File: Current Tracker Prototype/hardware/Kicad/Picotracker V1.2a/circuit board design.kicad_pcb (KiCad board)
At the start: 2 copper layers, 33.3 x 20.1 mm, 31 parts, among them J1 Conn_01x10, J2 GND, J3 3.3V, J4 ICSS Logo, J5 Conn_01x01, Q1 IRLML6402, SW1 SW_Push, U1 MAX-M8C, U3 CMWX1ZZABZ-078, U6 MS5607-02BA

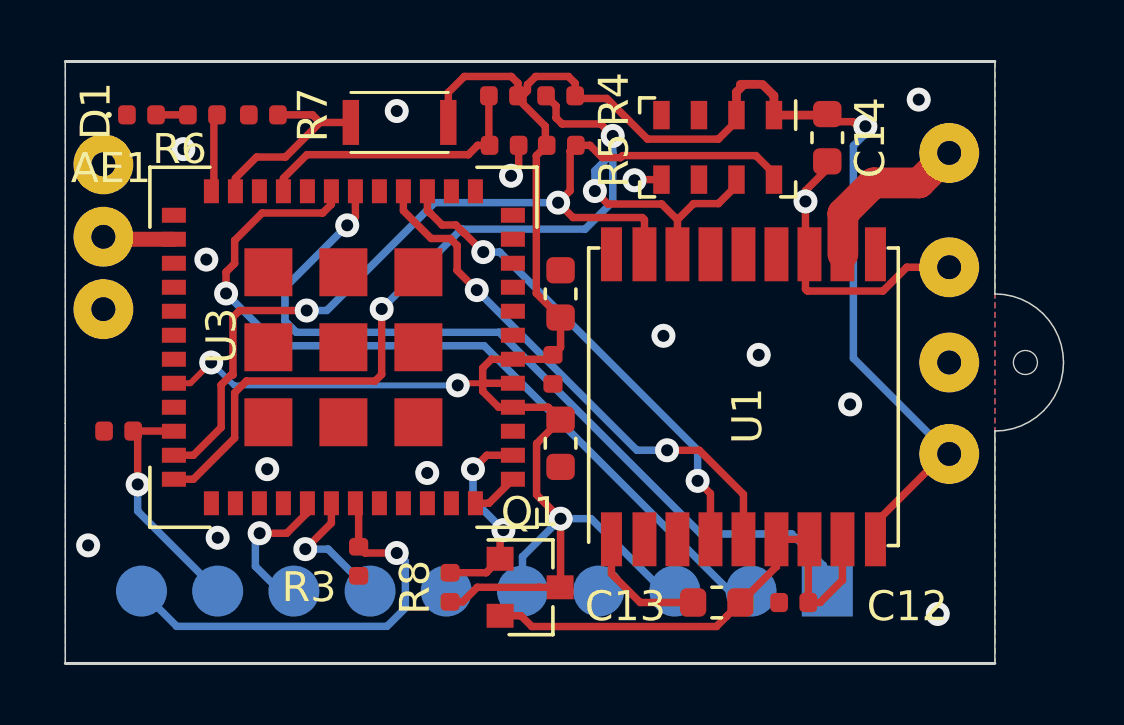
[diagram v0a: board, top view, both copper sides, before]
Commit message: Put in P channel MOSFET
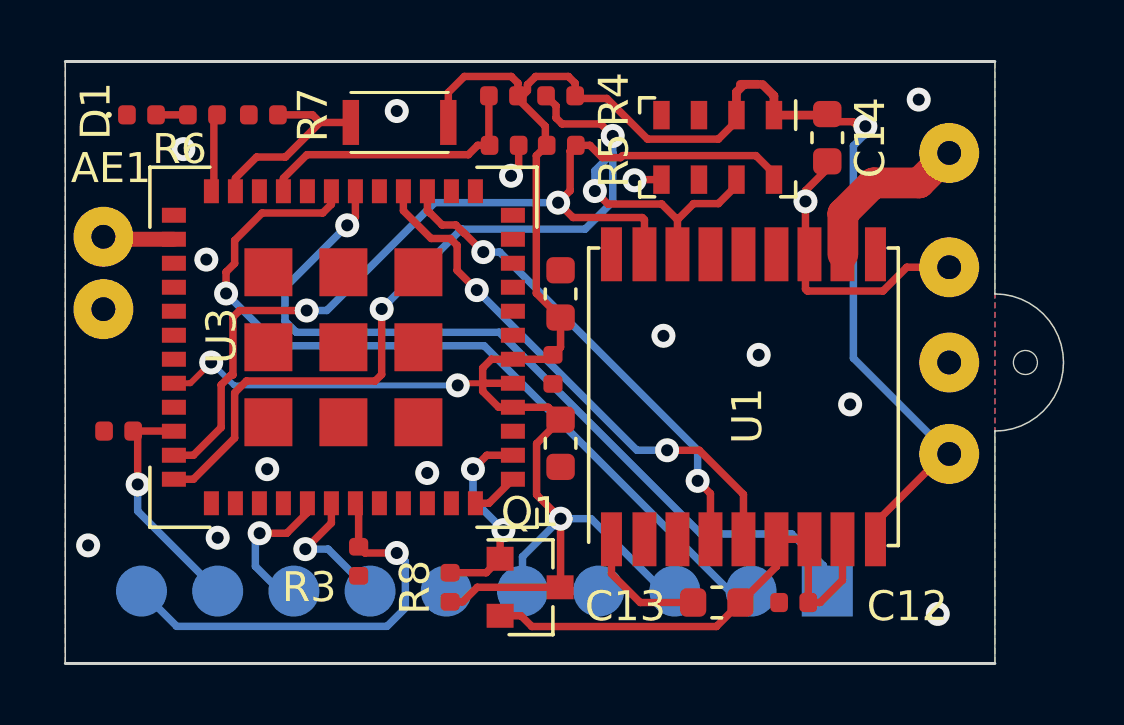
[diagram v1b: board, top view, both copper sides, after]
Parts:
- removed the J5 at (268.0, 163.4)
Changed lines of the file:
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@@
     (thickness 0.4)
     (drawings 24)
-    (tracks 293)
+    (tracks 291)
     (zones 0)
-    (modules 31)
+    (modules 30)
     (nets 22)
   )
@@
     (add_net "Net-(C12-Pad1)")
     (add_net "Net-(D1-Pad2)")
+    (add_net "Net-(SolarCellMount1-Pad1)")
+    (add_net "Net-(U1-Pad13)")
+    (add_net "Net-(U1-Pad14)")
+    (add_net "Net-(U1-Pad15)")
+    (add_net "Net-(U1-Pad18)")
+    (add_net "Net-(U1-Pad2)")
+    (add_net "Net-(U1-Pad3)")
+    (add_net "Net-(U3-Pad10)")
+    (add_net "Net-(U3-Pad11)")
+    (add_net "Net-(U3-Pad12)")
+    (add_net "Net-(U3-Pad13)")
+    (add_net "Net-(U3-Pad14)")
+    (add_net "Net-(U3-Pad17)")
+    (add_net "Net-(U3-Pad20)")
+    (add_net "Net-(U3-Pad22)")
+    (add_net "Net-(U3-Pad28)")
+    (add_net "Net-(U3-Pad29)")
+    (add_net "Net-(U3-Pad30)")
+    (add_net "Net-(U3-Pad31)")
+    (add_net "Net-(U3-Pad33)")
+    (add_net "Net-(U3-Pad37)")
+    (add_net "Net-(U3-Pad38)")
+    (add_net "Net-(U3-Pad39)")
+    (add_net "Net-(U3-Pad40)")
+    (add_net "Net-(U3-Pad45)")
+    (add_net "Net-(U3-Pad46)")
+    (add_net "Net-(U3-Pad47)")
+    (add_net "Net-(U3-Pad8)")
+    (add_net "Net-(U3-Pad9)")
+    (add_net "Net-(U6-Pad6)")
   )
   (net_class Power ""
@@
       (rotate (xyz 0 0 0))
     )
-  )
-  (module Connector_Wire:SolderWirePad_1x01_Drill0.8mm (layer F.Cu)
-    (at 267.97 163.449)
-    (descr "Wire solder connection")
-    (tags connector)
-    (attr virtual)
-    (fp_text reference J5 (at -2.667 -0.635) (layer F.SilkS) hide
-      (effects (font (size 1 1) (thickness 0.15)))
-    )
-    (fp_text value Conn_01x01 (at 0 2.54) (layer F.Fab)
-      (effects (font (size 1 1) (thickness 0.15)))
-    )
-    (fp_text user %R (at 0 0) (layer F.Fab)
-      (effects (font (size 1 1) (thickness 0.15)))
-    )
-    (fp_line (start -1.5 -1.5) (end 1.5 -1.5) (layer F.CrtYd) (width 0.05))
-    (fp_line (start -1.5 -1.5) (end -1.5 1.5) (layer F.CrtYd) (width 0.05))
-    (fp_line (start 1.5 1.5) (end 1.5 -1.5) (layer F.CrtYd) (width 0.05))
-    (fp_line (start 1.5 1.5) (end -1.5 1.5) (layer F.CrtYd) (width 0.05))
-    (pad 1 thru_hole circle (at 0 0) (size 1.99898 1.99898) (drill 0.8001) (layers *.Cu *.Mask)
-      (net 1 GND))
   )
   (module Connector_Wire:SolderWirePad_1x01_Drill0.8mm (layer F.Cu)
@@
   (segment (start 271.563 170.053) (end 270.871 170.745) (width 0.2) (layer F.Cu) (net 2))
   (segment (start 283.321 175.371) (end 283.21 175.26) (width 0.25) (layer F.Cu) (net 2))
-  (segment (start 282.494 177.546) (end 283.194 177.546) (width 0.25) (layer F.Cu) (net 2))
-  (segment (start 280.432 177.546) (end 282.494 177.546) (width 0.25) (layer F.Cu) (net 2))
+  (segment (start 280.432 177.546) (end 283.194 177.546) (width 0.25) (layer F.Cu) (net 2) (status 20))
   (segment (start 279.947 178.031) (end 280.432 177.546) (width 0.25) (layer F.Cu) (net 2))
-  (segment (start 279.527 178.031) (end 279.947 178.031) (width 0.25) (layer F.Cu) (net 2))
-  (segment (start 283.21 177.53) (end 283.194 177.546) (width 0.25) (layer F.Cu) (net 2))
-  (segment (start 283.21 175.26) (end 283.21 177.53) (width 0.25) (layer F.Cu) (net 2))
+  (segment (start 279.527 178.031) (end 279.947 178.031) (width 0.25) (layer F.Cu) (net 2) (status 10))
+  (segment (start 283.21 177.53) (end 283.194 177.546) (width 0.25) (layer F.Cu) (net 2) (status 30))
+  (segment (start 283.21 175.26) (end 283.21 177.53) (width 0.25) (layer F.Cu) (net 2) (status 20))
   (segment (start 289.072 164.157) (end 289.072 163.957) (width 0.25) (layer F.Cu) (net 3) (status 30))
   (segment (start 288.471999 164.757001) (end 289.072 164.157) (width 0.25) (layer F.Cu) (net 3) (status 20))
@@
   (segment (start 291.465 178.054) (end 291.86 178.054) (width 0.25) (layer F.Cu) (net 20) (status 10))
   (segment (start 290.406 175.946) (end 291.506 175.946) (width 0.25) (layer F.Cu) (net 20) (status 30))
-  (segment (start 288.742888 178.515612) (end 289.2045 178.054) (width 0.25) (layer F.Cu) (net 20))
-  (segment (start 288.40449 178.85401) (end 288.742888 178.515612) (width 0.25) (layer F.Cu) (net 20))
+  (segment (start 288.40449 178.85401) (end 289.2045 178.054) (width 0.25) (layer F.Cu) (net 20) (status 20))
   (segment (start 282.25201 178.85401) (end 288.40449 178.85401) (width 0.25) (layer F.Cu) (net 20))
   (segment (start 281.894 178.496) (end 282.25201 178.85401) (width 0.25) (layer F.Cu) (net 20))
-  (segment (start 281.194 178.496) (end 281.894 178.496) (width 0.25) (layer F.Cu) (net 20))
+  (segment (start 281.194 178.496) (end 281.894 178.496) (width 0.25) (layer F.Cu) (net 20) (status 10))
   (via (at 280.289 173.609) (size 0.8) (drill 0.4) (layers F.Cu B.Cu) (net 21))
   (segment (start 281.621 173.145) (end 280.753 173.145) (width 0.25) (layer F.Cu) (net 21) (status 10))
@@
   (segment (start 280.289 174.625) (end 281.305 175.641) (width 0.25) (layer B.Cu) (net 21))
   (segment (start 281.194 175.752) (end 281.305 175.641) (width 0.25) (layer F.Cu) (net 21))
-  (segment (start 281.194 176.596) (end 281.194 175.752) (width 0.25) (layer F.Cu) (net 21))
-  (segment (start 280.729 177.061) (end 281.194 176.596) (width 0.25) (layer F.Cu) (net 21))
-  (segment (start 279.527 177.061) (end 280.729 177.061) (width 0.25) (layer F.Cu) (net 21))
+  (segment (start 281.194 176.596) (end 281.194 175.752) (width 0.25) (layer F.Cu) (net 21) (status 10))
+  (segment (start 280.729 177.061) (end 281.194 176.596) (width 0.25) (layer F.Cu) (net 21) (status 20))
+  (segment (start 279.527 177.061) (end 280.729 177.061) (width 0.25) (layer F.Cu) (net 21) (status 10))
   (zone (net 1) (net_name GND) (layer F.Cu) (hatch edge 0.508)
     (connect_pads (clearance 0.15))

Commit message: rotated p channel mosfet
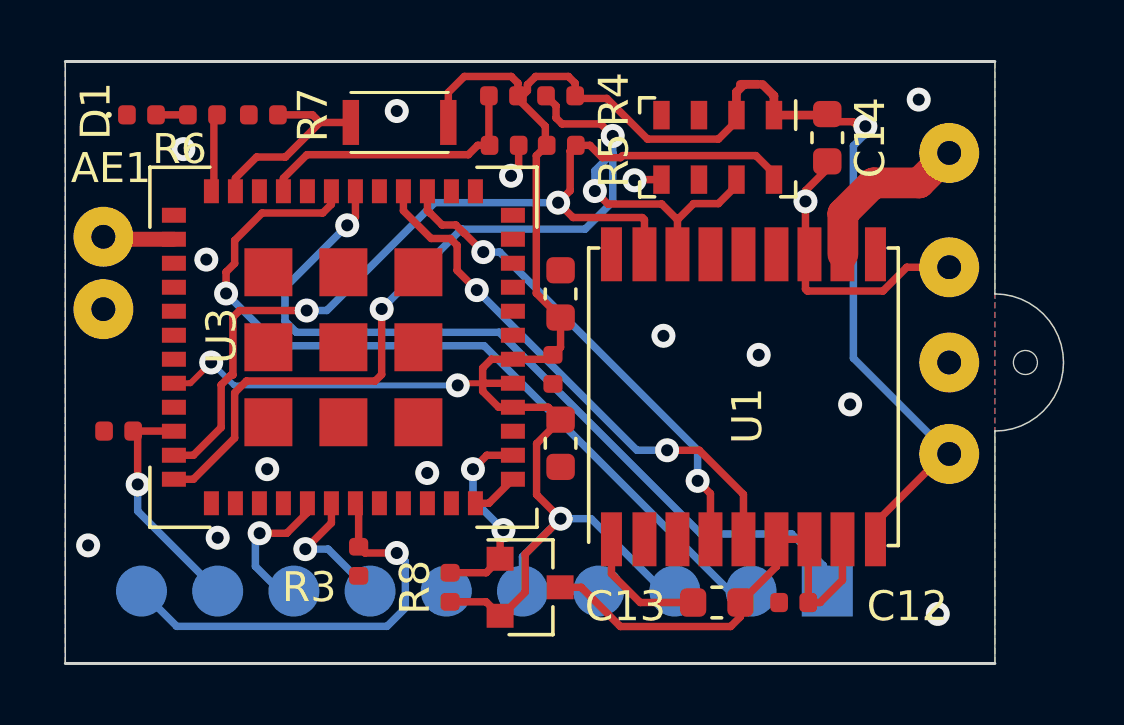
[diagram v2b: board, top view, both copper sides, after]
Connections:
- Q1 pad 2: Net-(C12-Pad1) -> +3V3
- Q1 pad 3: +3V3 -> Net-(C12-Pad1)
- SolarCellMount1 pad 1: (no net) -> Net-(SolarCellMount1-Pad1)
- U1 pad 13: (no net) -> Net-(U1-Pad13)
- U1 pad 14: (no net) -> Net-(U1-Pad14)
- U1 pad 15: (no net) -> Net-(U1-Pad15)
- U1 pad 18: (no net) -> Net-(U1-Pad18)
- U1 pad 2: (no net) -> Net-(U1-Pad2)
- U1 pad 3: (no net) -> Net-(U1-Pad3)
- U3 pad 10: (no net) -> Net-(U3-Pad10)
- U3 pad 11: (no net) -> Net-(U3-Pad11)
- U3 pad 12: (no net) -> Net-(U3-Pad12)
- U3 pad 13: (no net) -> Net-(U3-Pad13)
- U3 pad 14: (no net) -> Net-(U3-Pad14)
- U3 pad 17: (no net) -> Net-(U3-Pad17)
- U3 pad 20: (no net) -> Net-(U3-Pad20)
- U3 pad 22: (no net) -> Net-(U3-Pad22)
- U3 pad 28: (no net) -> Net-(U3-Pad28)
- U3 pad 29: (no net) -> Net-(U3-Pad29)
- U3 pad 30: (no net) -> Net-(U3-Pad30)
- U3 pad 31: (no net) -> Net-(U3-Pad31)
- U3 pad 33: (no net) -> Net-(U3-Pad33)
- U3 pad 37: (no net) -> Net-(U3-Pad37)
- U3 pad 38: (no net) -> Net-(U3-Pad38)
- U3 pad 39: (no net) -> Net-(U3-Pad39)
- U3 pad 40: (no net) -> Net-(U3-Pad40)
- U3 pad 45: (no net) -> Net-(U3-Pad45)
- U3 pad 46: (no net) -> Net-(U3-Pad46)
- U3 pad 47: (no net) -> Net-(U3-Pad47)
- U3 pad 8: (no net) -> Net-(U3-Pad8)
- U3 pad 9: (no net) -> Net-(U3-Pad9)
- U6 pad 6: (no net) -> Net-(U6-Pad6)
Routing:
- net Net-(C12-Pad1): track 17.1 -> 15.8 mm
